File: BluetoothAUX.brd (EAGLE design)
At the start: 22.2 x 24.4 mm, 19 parts, among them IC2 TPA6132A2, J3 AUDIO_JACK_TRRSSMD_RA, J4 USB, Q1 FDV301N

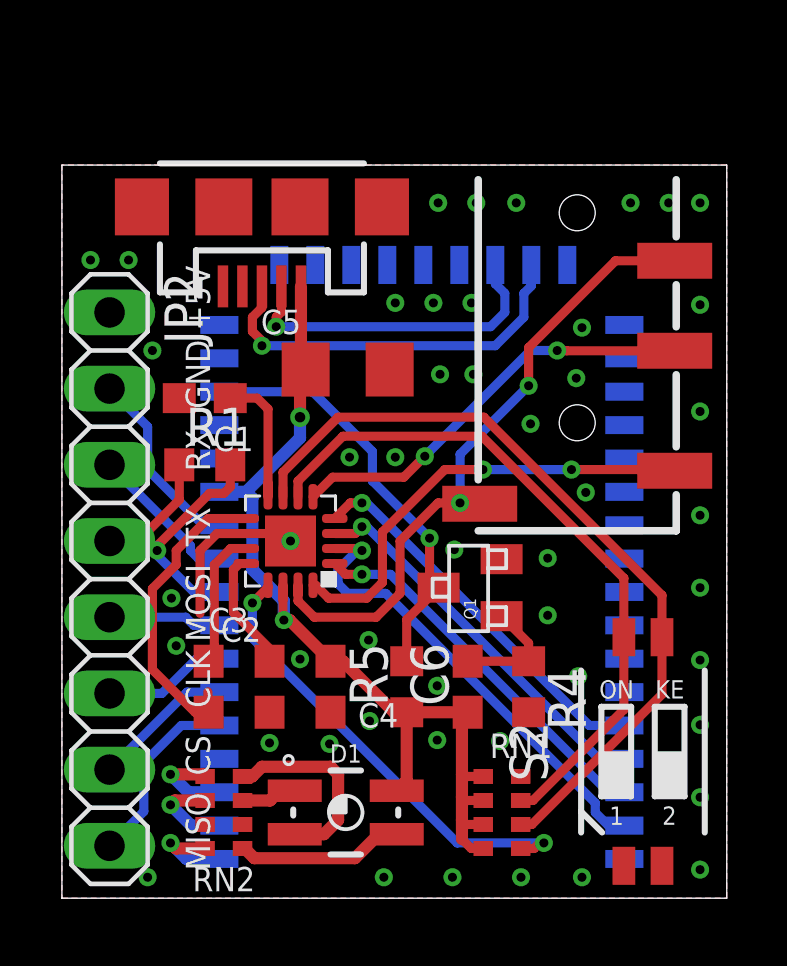
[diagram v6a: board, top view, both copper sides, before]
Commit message: Remove UART, add silk
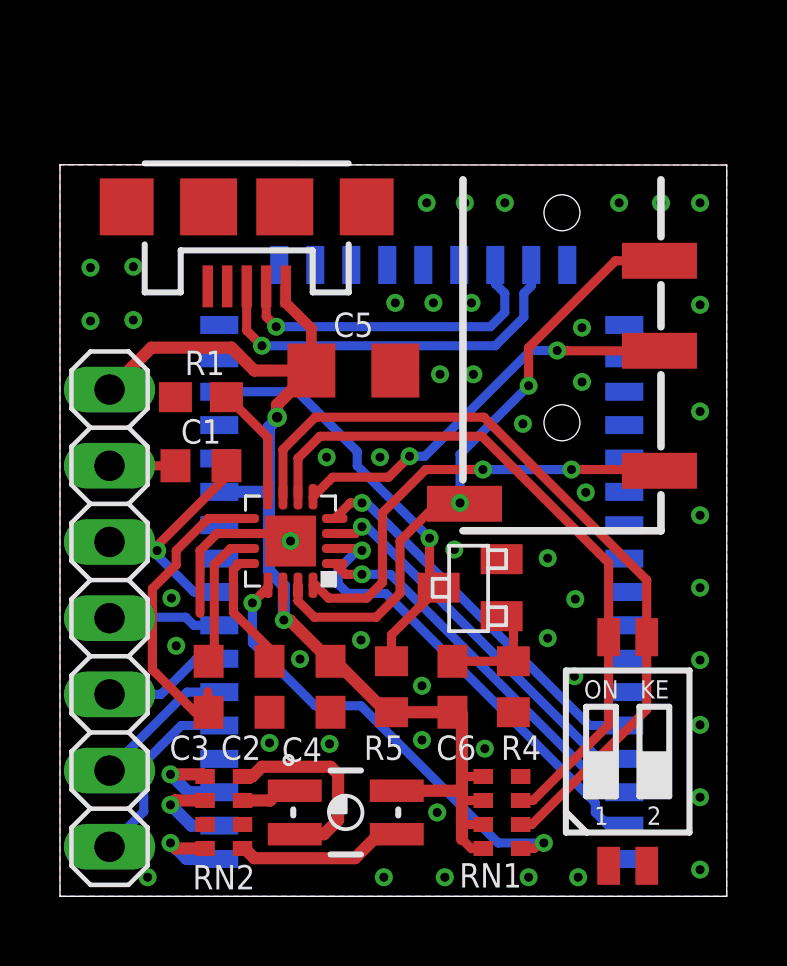
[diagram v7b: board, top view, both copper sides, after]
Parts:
- removed JP2: (no value), pinhead:1X08
- added JP1: (no value), pinhead:1X07
- moved J3 0.51 mm to (88.7, 45.7)
- moved C6 0.51 mm to (85.1, 28.3)
- moved J4 0.51 mm to (78.2, 44.3)
- moved R4 0.51 mm to (87.1, 28.3)
- moved R5 0.51 mm to (83.1, 28.3)
- moved S2 0.51 mm to (90.9, 26.2)
- moved C5 0.19 mm to (81.8, 38.9)
- moved C1 0.13 mm to (76.7, 38.0)
- moved R1 0.13 mm to (76.7, 35.7)
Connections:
- removed net RX: JP2.2, U$1.P$11
- removed net SPI_PCM: JP2.4, R1.1
- removed net TX: JP2.3, U$1.P$10
- new net N$6: JP1.2, R1.1
- net +5V: now also JP1.1
- net CLK: now also JP1.5; no longer JP2.6
- net CS: now also JP1.6; no longer JP2.7
- net GND: now also JP1.3; no longer JP2.1
- net MISO: now also JP1.7; no longer JP2.8
- net MOSI: now also JP1.4; no longer JP2.5
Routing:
- net +5V: track 34.1 -> 41.2 mm
- net RX: track 6.38 -> 0.00 mm
- net TX: track 5.05 -> 0.00 mm
- net SPI_PCM: track 4.06 -> 0.00 mm
- net N$6: track 0.00 -> 2.20 mm
- net OUTL: track 15.0 -> 15.9 mm
- net OUTR: track 14.1 -> 13.6 mm
- net GND: vias 48 -> 50
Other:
- board text added: "SPI"
- board text added: "github.com/autowp/BluetoothAUX"
- board text added: "v0.4 2017.10.17"
- board text removed: "RX"
- board text removed: "TX"

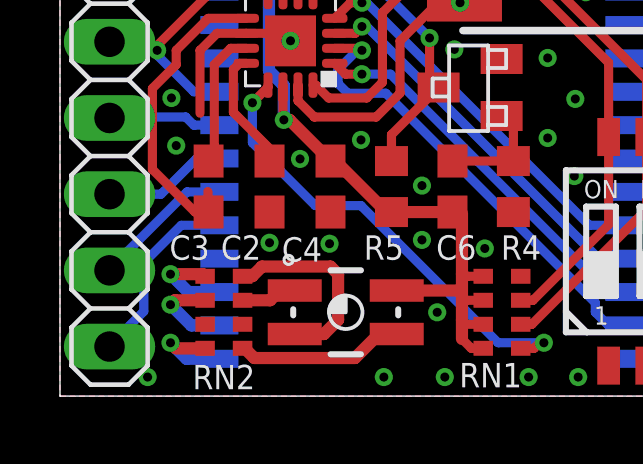
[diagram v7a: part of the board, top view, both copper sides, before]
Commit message: Improve silk
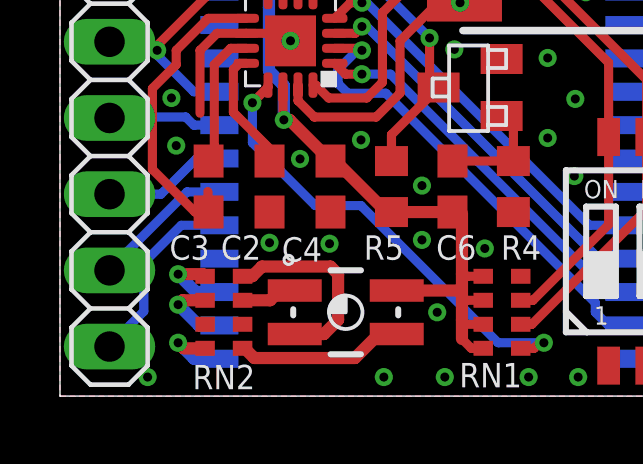
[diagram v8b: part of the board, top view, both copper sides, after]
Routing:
- net RED: track 3.13 -> 2.62 mm
- net GREEN: track 3.06 -> 2.55 mm
- net BLUE: track 3.08 -> 2.57 mm
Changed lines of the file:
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@@
 <grid distance="0.01" unitdist="inch" unit="inch" style="lines" multiple="1" display="yes" altdistance="0.005" altunitdist="inch" altunit="inch"/>
 <layers>
-<layer number="1" name="Top" color="4" fill="1" visible="no" active="yes"/>
+<layer number="1" name="Top" color="4" fill="1" visible="yes" active="yes"/>
 <layer number="16" name="Bottom" color="1" fill="1" visible="yes" active="yes"/>
 <layer number="17" name="Pads" color="2" fill="1" visible="yes" active="yes"/>
@@
 <contactref element="U$1" pad="P$1"/>
 <contactref element="RN2" pad="8"/>
-<via x="75.692" y="23.114" extent="1-16" drill="0.3"/>
-<wire x1="75.692" y1="23.114" x2="76.226" y2="22.58" width="0.4064" layer="16"/>
-<wire x1="76.226" y1="22.58" x2="77.32" y2="22.58" width="0.4064" layer="16"/>
-<wire x1="76.845" y1="22.93" x2="75.876" y2="22.93" width="0.4064" layer="1"/>
-<wire x1="75.876" y1="22.93" x2="75.692" y2="23.114" width="0.4064" layer="1"/>
+<via x="75.946" y="23.114" extent="1-16" drill="0.3"/>
+<wire x1="75.946" y1="23.114" x2="76.48" y2="22.58" width="0.4064" layer="16"/>
+<wire x1="76.48" y1="22.58" x2="77.32" y2="22.58" width="0.4064" layer="16"/>
+<wire x1="76.845" y1="22.93" x2="76.13" y2="22.93" width="0.4064" layer="1"/>
+<wire x1="76.13" y1="22.93" x2="75.946" y2="23.114" width="0.4064" layer="1"/>
 </signal>
 <signal name="RED">
 <contactref element="U$1" pad="P$2"/>
 <contactref element="RN2" pad="6"/>
-<wire x1="76.845" y1="24.53" x2="75.838" y2="24.53" width="0.4064" layer="1"/>
-<wire x1="75.838" y1="24.53" x2="75.692" y2="24.384" width="0.4064" layer="1"/>
-<via x="75.692" y="24.384" extent="1-16" drill="0.3"/>
-<wire x1="75.692" y1="24.384" x2="76.3835" y2="23.6925" width="0.4064" layer="16"/>
-<wire x1="76.3835" y1="23.6925" x2="77.32" y2="23.6925" width="0.4064" layer="16"/>
+<wire x1="76.845" y1="24.53" x2="76.092" y2="24.53" width="0.4064" layer="1"/>
+<wire x1="76.092" y1="24.53" x2="75.946" y2="24.384" width="0.4064" layer="1"/>
+<via x="75.946" y="24.384" extent="1-16" drill="0.3"/>
+<wire x1="75.946" y1="24.384" x2="76.6375" y2="23.6925" width="0.4064" layer="16"/>
+<wire x1="76.6375" y1="23.6925" x2="77.32" y2="23.6925" width="0.4064" layer="16"/>
 </signal>
 <signal name="GREEN">
@@
 <contactref element="RN2" pad="5"/>
 <wire x1="76.845" y1="25.33" x2="76.775" y2="25.4" width="0.4064" layer="1"/>
-<wire x1="76.775" y1="25.4" x2="75.692" y2="25.4" width="0.4064" layer="1"/>
-<via x="75.692" y="25.4" extent="1-16" drill="0.3"/>
-<wire x1="75.692" y1="25.4" x2="76.287" y2="24.805" width="0.4064" layer="16"/>
-<wire x1="76.287" y1="24.805" x2="77.32" y2="24.805" width="0.4064" layer="16"/>
+<wire x1="76.775" y1="25.4" x2="75.946" y2="25.4" width="0.4064" layer="1"/>
+<via x="75.946" y="25.4" extent="1-16" drill="0.3"/>
+<wire x1="75.946" y1="25.4" x2="76.541" y2="24.805" width="0.4064" layer="16"/>
+<wire x1="76.541" y1="24.805" x2="77.32" y2="24.805" width="0.4064" layer="16"/>
 </signal>
 <signal name="BAT">
